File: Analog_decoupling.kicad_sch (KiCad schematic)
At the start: 123 parts, among them J1 22-23-2021, J2 22-23-2021, J3 22-23-2021, J4 302-S101, J5 OSTTC020162, U1 LT1129CST-5#PBF, U10 TLV9001IDBVR, U11 TLV9001IDBVR, U12 LP2985A-50DBVR, U13 LP2985A-50DBVR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

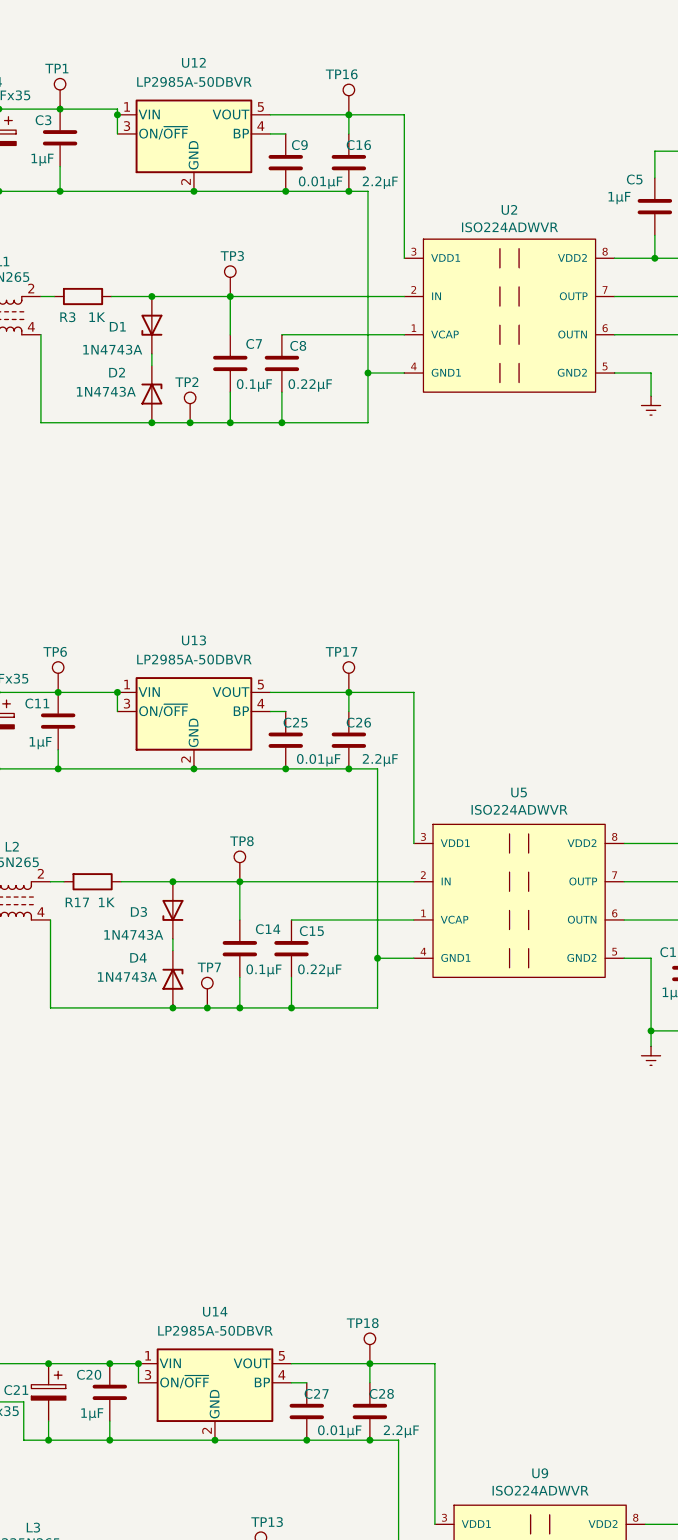
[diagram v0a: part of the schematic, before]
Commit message: GPIO port changed for input signals
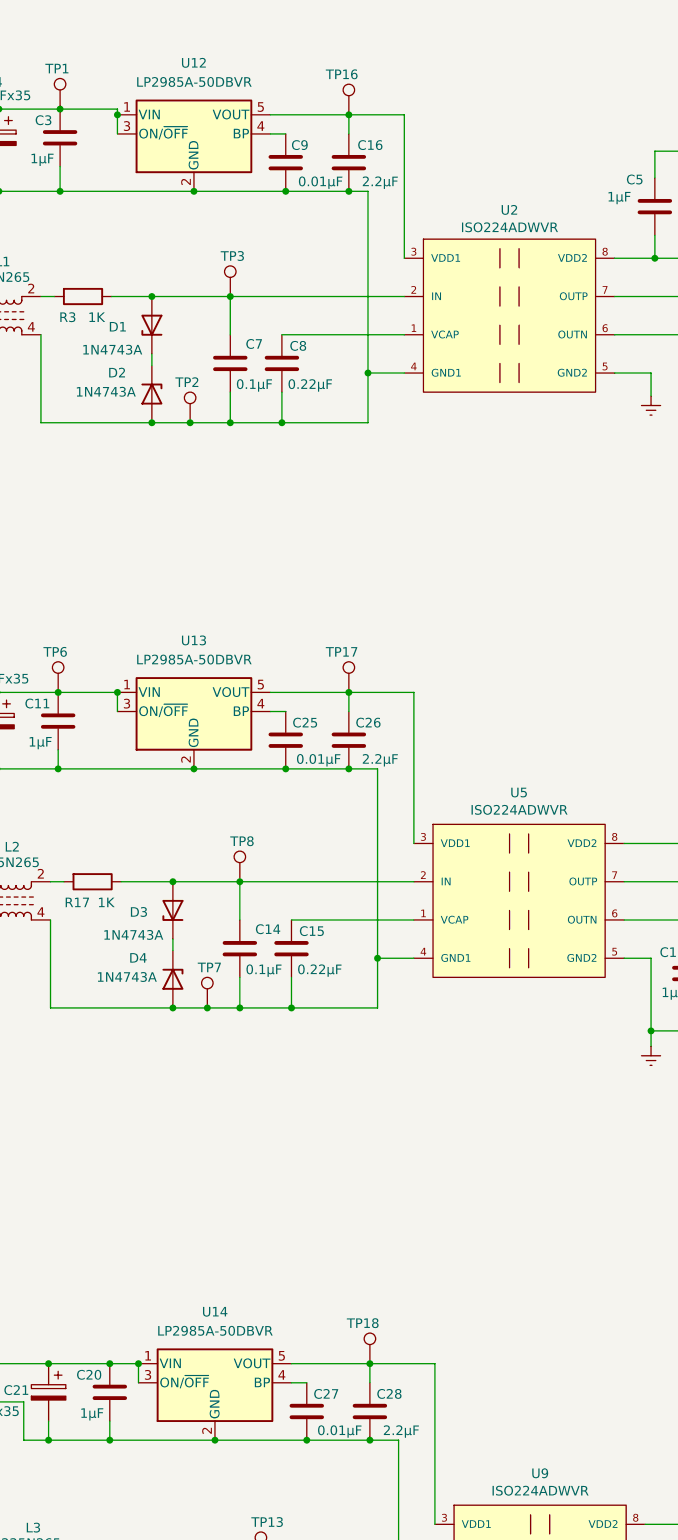
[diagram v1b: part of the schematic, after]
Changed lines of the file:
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@@
   (symbol (lib_id "Device:C") (at 132.588 212.09 0) (mirror y) (unit 1)
     (in_bom yes) (on_board yes)
-    (property "Reference" "C28" (id 0) (at 135.89 209.804 0)
+    (property "Reference" "C28" (id 0) (at 136.906 209.804 0)
       (effects (font (size 1.27 1.27)) (justify left))
     )
@@
   (symbol (lib_id "Device:C") (at 129.794 122.936 0) (mirror y) (unit 1)
     (in_bom yes) (on_board yes)
-    (property "Reference" "C26" (id 0) (at 132.842 120.65 0)
+    (property "Reference" "C26" (id 0) (at 134.112 120.65 0)
       (effects (font (size 1.27 1.27)) (justify left))
     )
@@
   (symbol (lib_id "Device:C") (at 121.412 122.936 0) (mirror y) (unit 1)
     (in_bom yes) (on_board yes)
-    (property "Reference" "C25" (id 0) (at 124.46 120.65 0)
+    (property "Reference" "C25" (id 0) (at 125.73 120.65 0)
       (effects (font (size 1.27 1.27)) (justify left))
     )
@@
   (symbol (lib_id "Device:C") (at 124.206 212.09 0) (mirror y) (unit 1)
     (in_bom yes) (on_board yes)
-    (property "Reference" "C27" (id 0) (at 127.254 209.804 0)
+    (property "Reference" "C27" (id 0) (at 128.524 209.804 0)
       (effects (font (size 1.27 1.27)) (justify left))
     )
@@
   (symbol (lib_id "Device:C") (at 129.794 46.228 0) (mirror y) (unit 1)
     (in_bom yes) (on_board yes)
-    (property "Reference" "C16" (id 0) (at 132.842 43.942 0)
-      (effects (font (size 1.27 1.27)) (justify left))
-    )
+    (property "Reference" "C16" (id 0) (at 134.366 43.942 0)
+      (effects (font (size 1.27 1.27)) (justify left))
+    )
